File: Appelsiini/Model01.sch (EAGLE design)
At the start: 55 parts

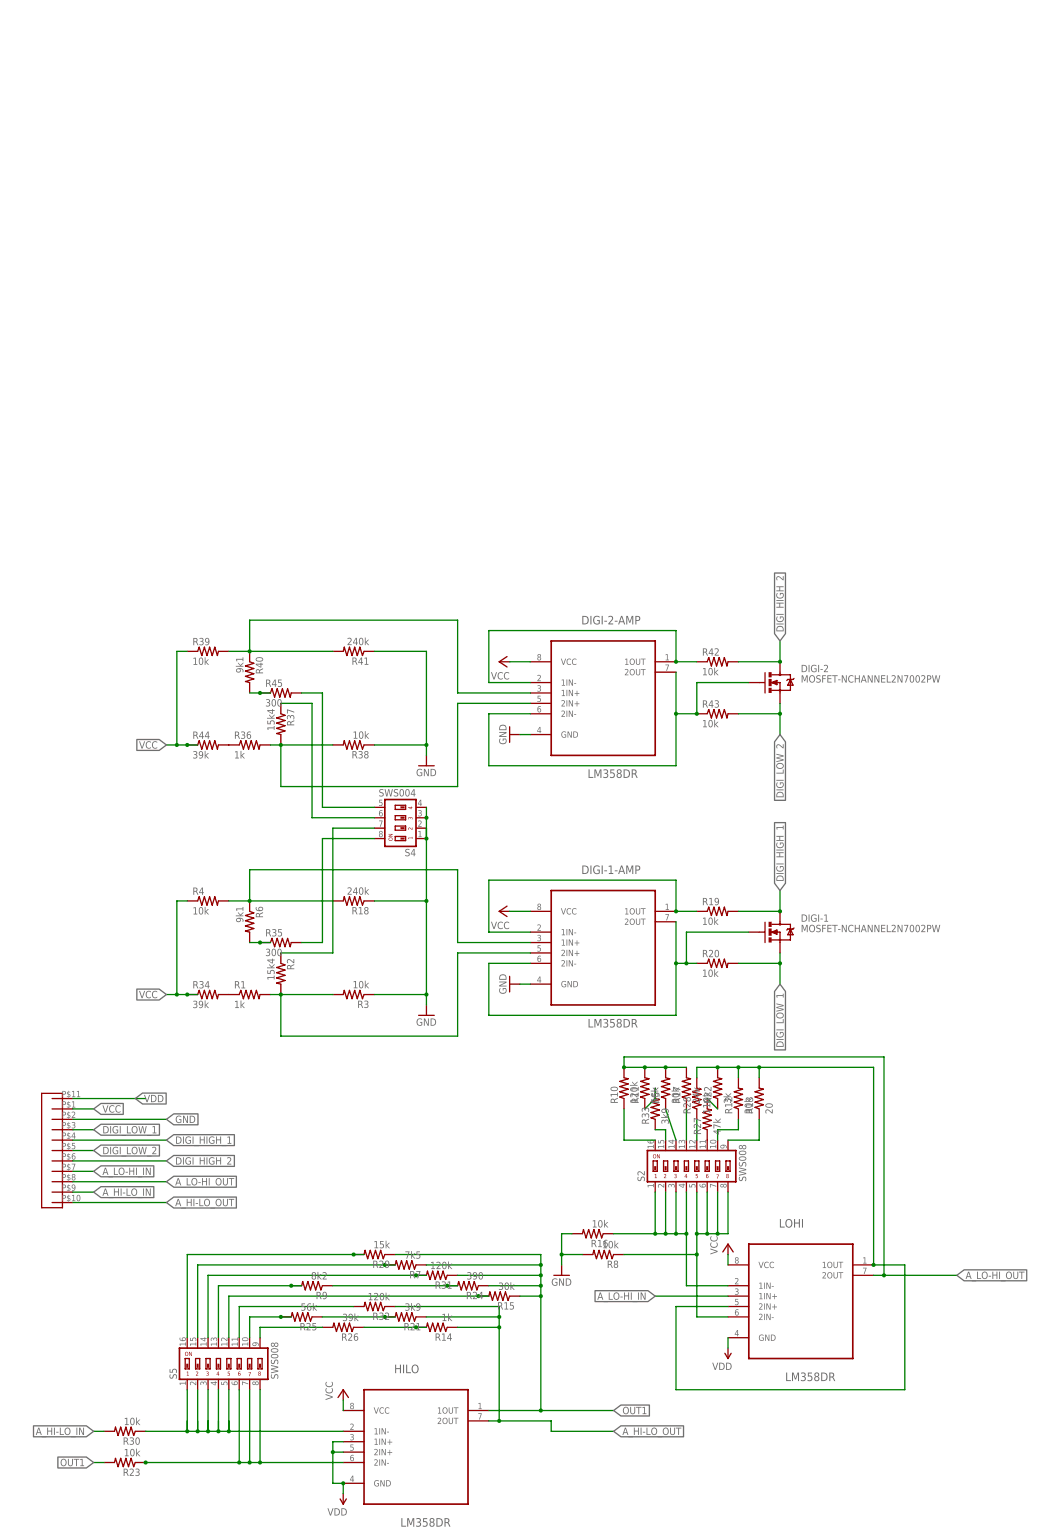
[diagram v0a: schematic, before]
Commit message: Add new version of website
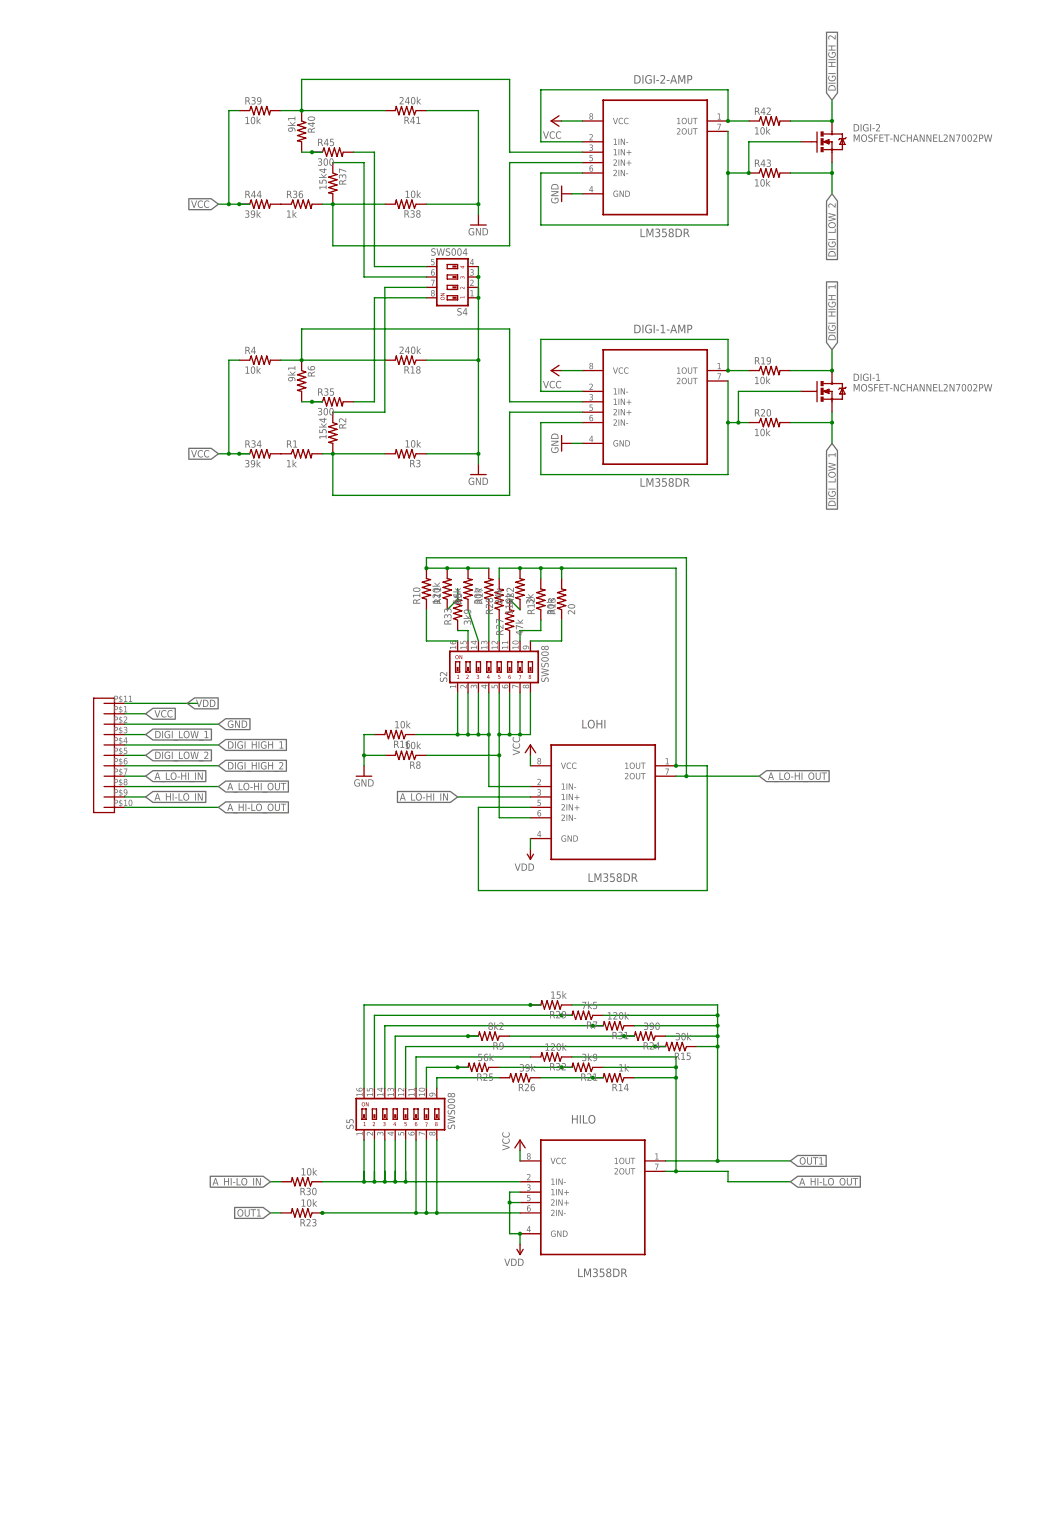
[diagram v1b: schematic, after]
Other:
- moved on the sheet: DIGI-1, DIGI-1-AMP, DIGI-2, DIGI-2-AMP, HILO, LOHI, R1, R10, R11, R12, R13, R14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
